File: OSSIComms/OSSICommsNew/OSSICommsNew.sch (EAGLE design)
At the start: 188 parts, among them Q1 NX-3215, U1 MAX2640, U10 MAX6369, U11 TPS3838, U12 MAX890L, U13 MCP1700_SOT23, U2 PE4259, U3 RF5110G, U4 OPA347, U5 MAX869L, U6 LMZ10503EXT, U7 ADF7021-N, U8 ADF7021-N, U9 MSP430F1611, X1 ESQ-126-38-G-D, X2 RFCON-MCX-R/A, X4 P-PAD-S, X5 5268-03, X6 P-PAD-S, X7 JTAG10PINMINI-H

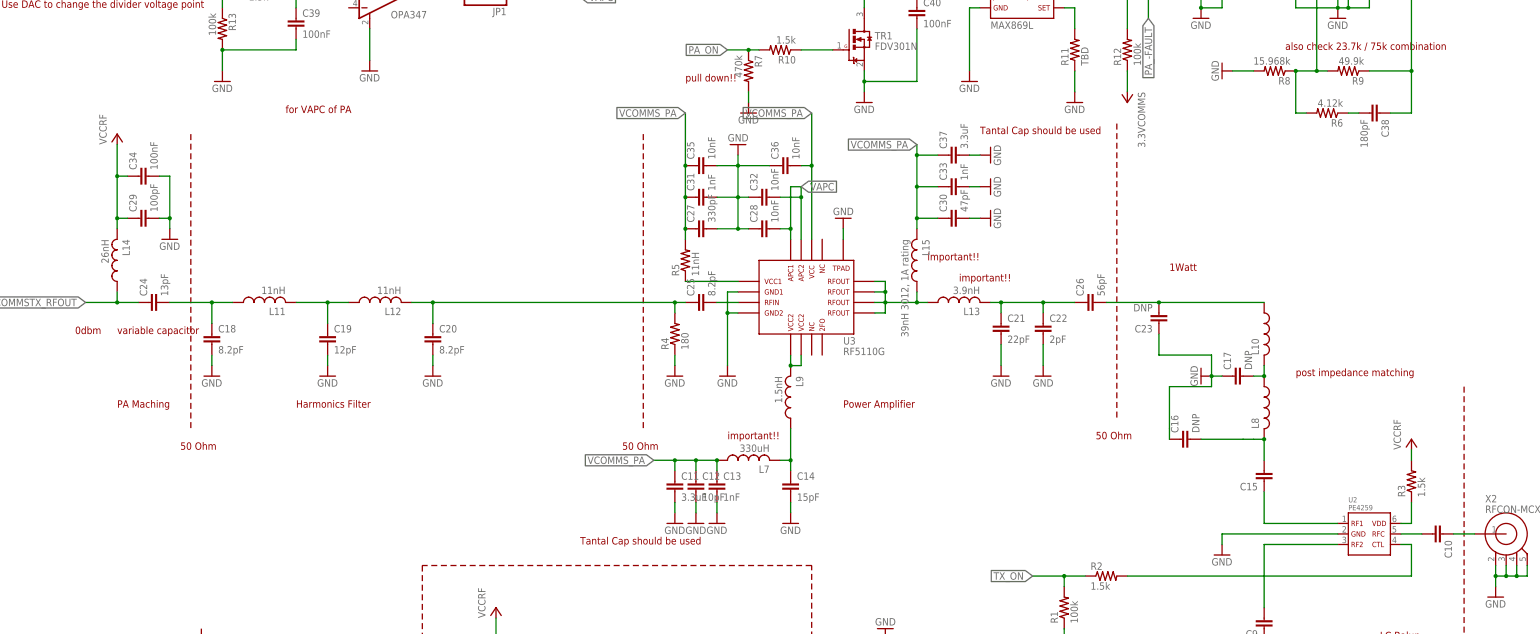
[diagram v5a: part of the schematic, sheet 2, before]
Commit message: COMMS PA setting fixed!
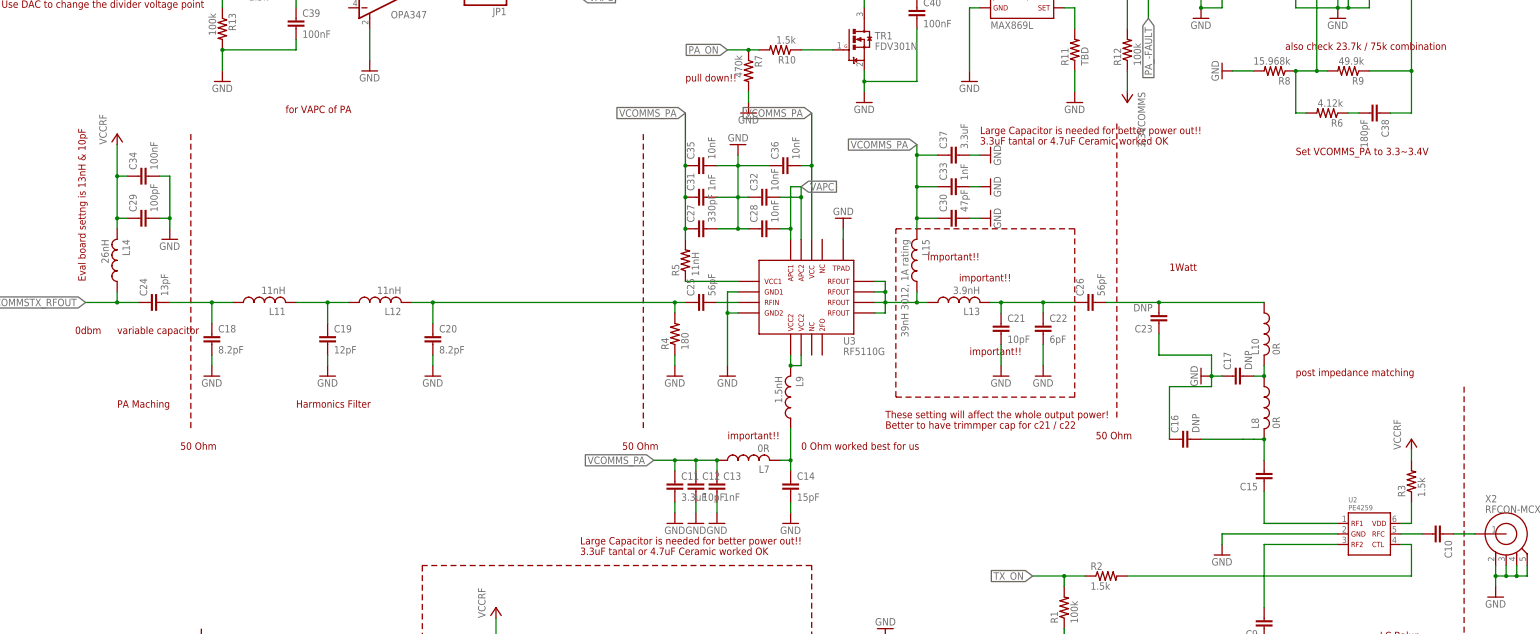
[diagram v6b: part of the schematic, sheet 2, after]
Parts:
- C21: value 22pF -> 10pF
- C22: value 2pF -> 6pF
- C25: value 8.2pF -> 56pF
- L10, L8: value (none) -> 0R
- L7: value 330uH -> 0R
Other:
- note added: "0 Ohm worked best for us"
- note added: "3.3uF tantal or 4.7uF Ceramic worked OK"
- note added: "Better to have trimmper cap for c21 / c22"
- note added: "Eval board settng is 13nH & 10pF"
- note added: "Large Capacitor is needed for better power out!!"
- note added: "Set VCOMMS_PA to 3.3~3.4V"
- note added: "These setting will affect the whole output power!"
- note removed: "Power Amplifier"
- note removed: "Tantal Cap should be used"
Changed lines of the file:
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@@
 <part name="X2" library="OSSI" deviceset="RFCON" device="-MCX-R/A"/>
 <part name="R4" library="OSSI" deviceset="R" device="0603(1608)" value="180"/>
-<part name="C25" library="OSSI" deviceset="C" device="0603(1608)" value="8.2pF"/>
+<part name="C25" library="OSSI" deviceset="C" device="0603(1608)" value="56pF"/>
 <part name="GND66" library="OSSI" deviceset="GND" device=""/>
 <part name="GND67" library="OSSI" deviceset="GND" device=""/>
@@
 <part name="GND69" library="OSSI" deviceset="GND" device=""/>
 <part name="GND70" library="OSSI" deviceset="GND" device=""/>
-<part name="C21" library="OSSI" deviceset="C" device="0603(1608)" value="22pF"/>
-<part name="C22" library="OSSI" deviceset="C" device="0603(1608)" value="2pF"/>
+<part name="C21" library="OSSI" deviceset="C" device="0603(1608)" value="10pF"/>
+<part name="C22" library="OSSI" deviceset="C" device="0603(1608)" value="6pF"/>
 <part name="C26" library="OSSI" deviceset="C" device="0603(1608)" value="56pF"/>
 <part name="GND71" library="OSSI" deviceset="GND" device=""/>
@@
 <part name="GND11" library="OSSI" deviceset="GND" device=""/>
 <part name="GND13" library="OSSI" deviceset="GND" device=""/>
-<part name="L10" library="OSSI" deviceset="L" device="0603(1608)"/>
-<part name="L8" library="OSSI" deviceset="L" device="0603(1608)"/>
+<part name="L10" library="OSSI" deviceset="L" device="0603(1608)" value="0R"/>
+<part name="L8" library="OSSI" deviceset="L" device="0603(1608)" value="0R"/>
 <part name="L6" library="OSSI" deviceset="L" device="0603(1608)"/>
 <part name="L4" library="OSSI" deviceset="L" device="0603(1608)"/>
@@
 <part name="R41" library="OSSI" deviceset="R" device="0603(1608)" value="0"/>
 <part name="C92" library="OSSI" deviceset="C" device="1210(3225)-GCM32" value="22uF,1210"/>
-<part name="L7" library="OSSI" deviceset="L" device="LQH32CN" value="330uH"/>
+<part name="L7" library="OSSI" deviceset="L" device="LQH32CN" value="0R"/>
 <part name="R14" library="OSSI" deviceset="R" device="0603(1608)" value="1.5k"/>
 <part name="R7" library="OSSI" deviceset="R" device="0603(1608)" value="470k"/>
@@
 <text x="38.1" y="147.32" size="1.778" layer="94">variable capacitor</text>
 <text x="38.1" y="60.96" size="1.778" layer="94">variable capacitor</text>
-<text x="246.38" y="195.58" size="1.778" layer="94">Tantal Cap should be used</text>
 <wire x1="165.1" y1="195.58" x2="165.1" y2="124.46" width="0.1524" layer="94" style="shortdash"/>
 <text x="160.02" y="119.38" size="1.778" layer="94">50 Ohm</text>
 <wire x1="279.4" y1="198.12" x2="279.4" y2="127" width="0.1524" layer="94" style="shortdash"/>
 <text x="274.32" y="121.92" size="1.778" layer="94">50 Ohm</text>
-<text x="213.36" y="129.54" size="1.778" layer="94">Power Amplifier </text>
-<text x="149.86" y="96.52" size="1.778" layer="94">Tantal Cap should be used</text>
 <wire x1="58.42" y1="76.2" x2="58.42" y2="5.08" width="0.1524" layer="94" style="shortdash"/>
 <text x="53.34" y="0" size="1.778" layer="94">50 Ohm</text>
@@
 <text x="147.32" y="30.48" size="1.778" layer="94">15.5dB Gain Measured @ these values</text>
 <text x="147.32" y="27.94" size="1.778" layer="94">15pF / 47nH / 1500pF will give similar results</text>
+<text x="203.2" y="119.38" size="1.778" layer="94">0 Ohm worked best for us</text>
+<text x="246.38" y="193.04" size="1.778" layer="94">3.3uF tantal or 4.7uF Ceramic worked OK</text>
+<text x="149.86" y="93.98" size="1.778" layer="94">3.3uF tantal or 4.7uF Ceramic worked OK</text>
+<text x="149.86" y="96.52" size="1.778" layer="94">Large Capacitor is needed for better power out!!</text>
+<text x="246.38" y="195.58" size="1.778" layer="94">Large Capacitor is needed for better power out!!</text>
+<wire x1="226.06" y1="172.72" x2="269.24" y2="172.72" width="0.1524" layer="94" style="shortdash"/>
+<wire x1="269.24" y1="172.72" x2="269.24" y2="132.08" width="0.1524" layer="94" style="shortdash"/>
+<wire x1="269.24" y1="132.08" x2="226.06" y2="132.08" width="0.1524" layer="94" style="shortdash"/>
+<wire x1="226.06" y1="132.08" x2="226.06" y2="172.72" width="0.1524" layer="94" style="shortdash"/>
+<text x="223.52" y="127" size="1.778" layer="94">These setting will affect the whole output power!</text>
+<text x="243.84" y="142.24" size="1.778" layer="94">important!!</text>
+<text x="223.52" y="124.46" size="1.778" layer="94">Better to have trimmper cap for c21 / c22</text>
+<text x="30.48" y="160.02" size="1.778" layer="94" rot="R90">Eval board settng is 13nH &amp; 10pF</text>
+<text x="322.58" y="190.5" size="1.778" layer="94">Set VCOMMS_PA to 3.3~3.4V</text>
 </plain>
 <instances>

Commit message: all values for tuned results are updated
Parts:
- C24: value 13pF -> 6pF
- L14: value 26nH -> 27nH
- L16: value 0 Ohm -> 7R, 3A, Ferrite bead
- R42: value TBD -> 6.2k
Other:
- note added: "10pF +6pF is better than 16 pF why???"
- note added: "110 is used"
- note added: "222.5mA limit"
- note added: "22uF added!!"
- note added: "Change this to LM7321"
- note added: "Current drive capability should be larger!!!"
- note added: "Set to 2.25V for 1W and best efficiency!!!"
- note added: "Use Tantal for larger RF out"
- note added: "tune RF switch to lower the insertion loss. currently around 1.2 dB loss!!!!"
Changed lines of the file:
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@@
 <part name="GND61" library="OSSI" deviceset="GND" device=""/>
 <part name="FRAME5" library="frames" deviceset="DINA3_L" device=""/>
-<part name="L14" library="OSSI" deviceset="L" device="0603(1608)" value="26nH"/>
+<part name="L14" library="OSSI" deviceset="L" device="0603(1608)" value="27nH"/>
 <part name="L11" library="OSSI" deviceset="L" device="0603(1608)" value="11nH"/>
 <part name="L12" library="OSSI" deviceset="L" device="0603(1608)" value="11nH"/>
@@
 <part name="U12" library="OSSI" deviceset="MAX890L" device=""/>
 <part name="GND6" library="OSSI" deviceset="GND" device=""/>
-<part name="R42" library="OSSI" deviceset="R" device="0603(1608)" value="TBD"/>
+<part name="R42" library="OSSI" deviceset="R" device="0603(1608)" value="6.2k"/>
 <part name="GND8" library="OSSI" deviceset="GND" device=""/>
 <part name="VBUS8" library="OSSI" deviceset="VBUS" device=""/>
@@
 <part name="GND14" library="OSSI" deviceset="GND" device=""/>
 <part name="GND15" library="OSSI" deviceset="GND" device=""/>
-<part name="C24" library="OSSI" deviceset="C" device="0603(1608)" value="13pF"/>
+<part name="C24" library="OSSI" deviceset="C" device="0603(1608)" value="6pF"/>
 <part name="C3" library="OSSI" deviceset="C" device="0603(1608)" value="13pF"/>
 <part name="C23" library="OSSI" deviceset="C" device="0603(1608)" value="DNP"/>
@@
 <part name="GND45" library="OSSI" deviceset="GND" device=""/>
 <part name="VCCRF2" library="OSSI" deviceset="VCCRF" device=""/>
-<part name="L16" library="OSSI" deviceset="L" device="0805(2012)" value="0 Ohm"/>
+<part name="L16" library="OSSI" deviceset="L" device="0805(2012)" value="7R, 3A, Ferrite bead"/>
 <part name="C91" library="OSSI" deviceset="C" device="0603(1608)" value="10nF"/>
 <part name="C93" library="OSSI" deviceset="C" device="0603(1608)" value="100nF"/>
@@
 <text x="30.48" y="160.02" size="1.778" layer="94" rot="R90">Eval board settng is 13nH &amp; 10pF</text>
 <text x="322.58" y="190.5" size="1.778" layer="94">Set VCOMMS_PA to 3.3~3.4V</text>
+<text x="106.68" y="215.9" size="1.778" layer="94">Current drive capability should be larger!!!</text>
+<text x="106.68" y="213.36" size="1.778" layer="94">Change this to LM7321</text>
+<text x="106.68" y="205.74" size="1.778" layer="94">Set to 2.25V for 1W and best efficiency!!!</text>
+<text x="200.66" y="93.98" size="1.778" layer="94">Use Tantal for larger RF out</text>
+<text x="256.54" y="190.5" size="1.778" layer="94">Use Tantal for larger RF out</text>
+<text x="223.52" y="121.92" size="1.778" layer="94">10pF +6pF  is better than 16 pF why???</text>
+<text x="325.12" y="127" size="1.778" layer="94">tune RF switch to lower the insertion loss. currently around 1.2 dB loss!!!!</text>
 </plain>
 <instances>
@@
 <text x="243.84" y="88.9" size="1.778" layer="94">0.8Vpp out with ac coupled capacitor</text>
 <text x="243.84" y="223.52" size="1.778" layer="94">0.8Vpp out with ac coupled capacitor</text>
+<text x="193.04" y="259.08" size="1.778" layer="94">22uF added!!</text>
+<text x="68.58" y="243.84" size="1.778" layer="94">110 is used</text>
+<text x="71.12" y="127" size="1.778" layer="94">110 is used</text>
 </plain>
 <instances>
@@
 <text x="111.76" y="243.84" size="1.778" layer="94">Pull Up open-drain /FAULT pin at the monitoring side VCC</text>
 <text x="281.94" y="246.38" size="1.778" layer="94">DIGITAL / RF POWER CHOKE</text>
+<text x="114.3" y="190.5" size="1.778" layer="94">222.5mA limit</text>
 </plain>
 <instances>

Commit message: comms value
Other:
- note added: "1500pF"
- note added: "47nH"
- note added: "8.2nH"
- note added: "Final Value but the result will be similar"
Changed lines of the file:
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@@
 <text x="256.54" y="190.5" size="1.778" layer="94">Use Tantal for larger RF out</text>
 <text x="223.52" y="121.92" size="1.778" layer="94">10pF +6pF  is better than 16 pF why???</text>
-<text x="325.12" y="127" size="1.778" layer="94">tune RF switch to lower the insertion loss. currently around 1.2 dB loss!!!!</text>
+<text x="299.72" y="116.84" size="1.778" layer="94">tune RF switch to lower the insertion loss. currently around 1.2 dB loss!!!!</text>
+<text x="193.04" y="50.8" size="1.778" layer="91">1500pF</text>
+<text x="180.34" y="50.8" size="1.778" layer="91">47nH</text>
+<text x="116.84" y="45.72" size="1.778" layer="91">8.2nH</text>
+<text x="116.84" y="43.18" size="1.778" layer="91">Final Value but the result will be similar</text>
 </plain>
 <instances>
